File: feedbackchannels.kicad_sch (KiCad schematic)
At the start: 81 parts, among them J18 FB CH1, J19 FB CH2, J20 FB CH3, J21 FB CH4, J22 VDET CH1, J23 VDET CH2, U21 TLP2366, U22 TLP2366, U23 TLP2366, U24 TLP2366, U25 TLP2366, U26 TLP2366, U27 TLV7031, U28 TLV7031, U30 TLP2366, U31 TLP2366, U32 74LVC1G126, U34 PCA9534, U35 SN74LVC541A

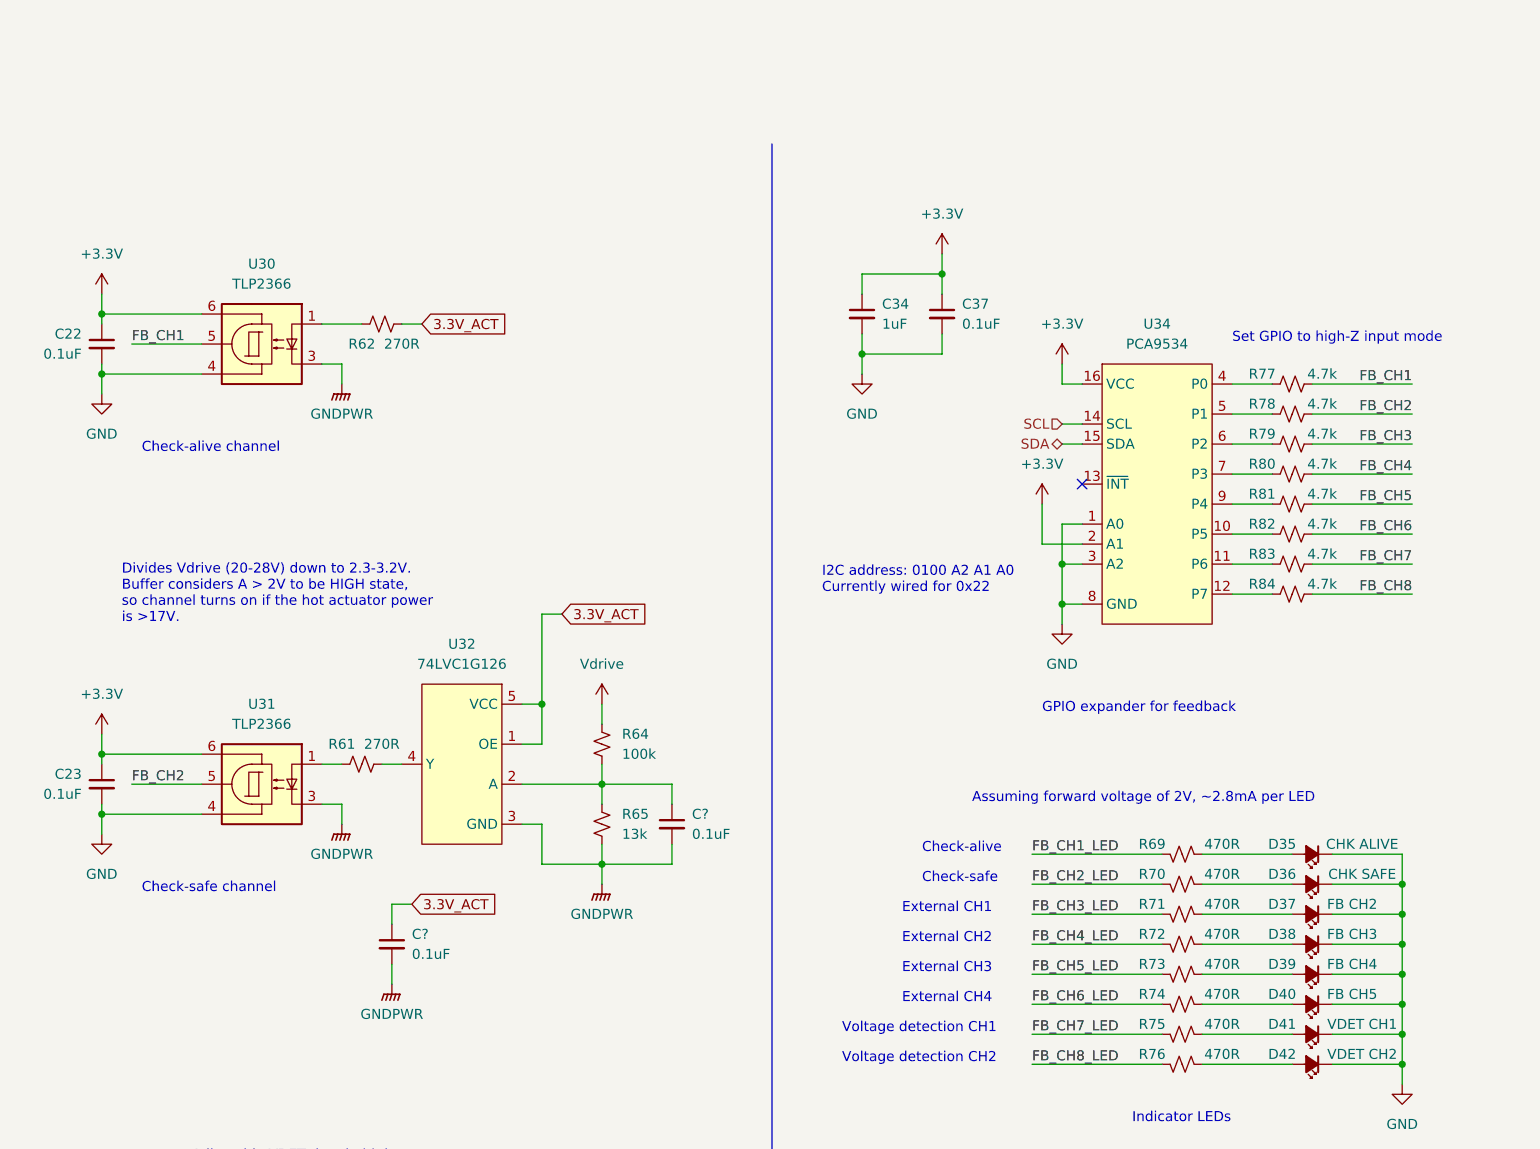
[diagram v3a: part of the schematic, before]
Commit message: LED MPNs and new status indicator
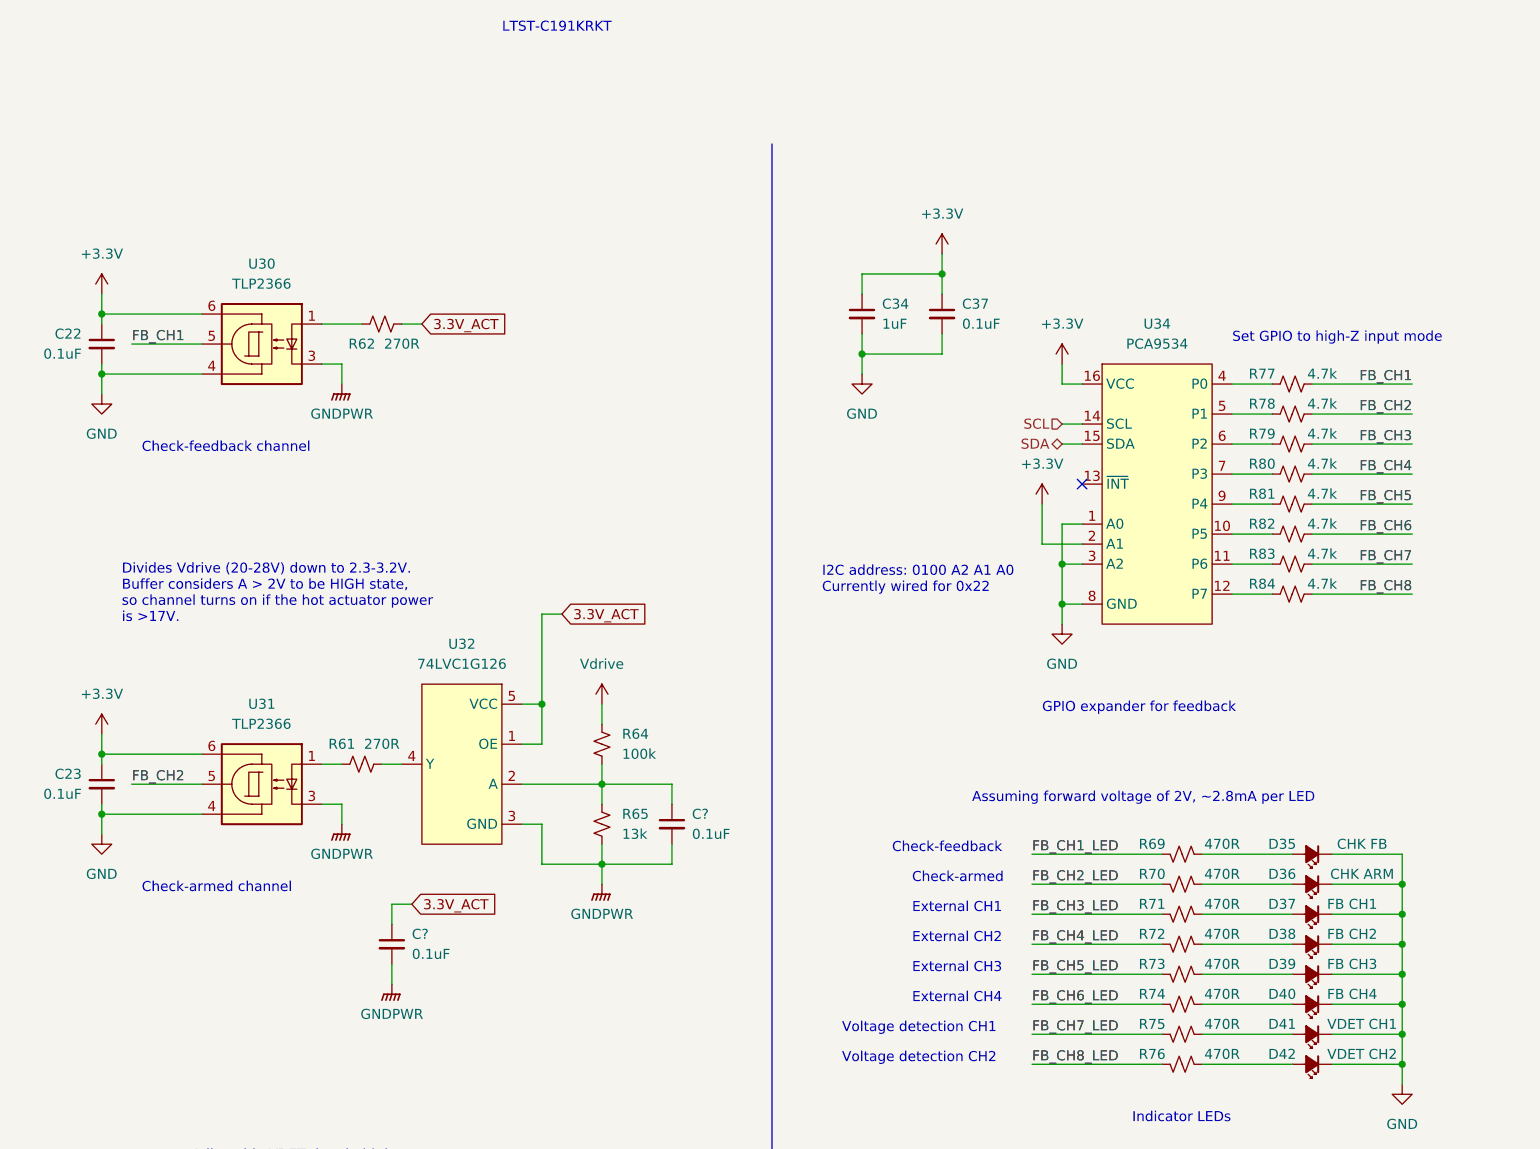
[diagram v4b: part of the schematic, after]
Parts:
- D35: value CHK ALIVE -> CHK FB; MPN (none) -> LTST-C191KGKT
- D36: value CHK SAFE -> CHK ARM; MPN (none) -> LTST-C191KFKT
- D37: value FB CH2 -> FB CH1; MPN (none) -> LTST-C191TBKT
- D38: value FB CH3 -> FB CH2; MPN (none) -> LTST-C191TBKT
- D39: value FB CH4 -> FB CH3; MPN (none) -> LTST-C191TBKT
- D40: value FB CH5 -> FB CH4; MPN (none) -> LTST-C191TBKT
- D41, D42: MPN (none) -> LTST-C191TBKT
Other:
- note added: "Check-armed"
- note added: "Check-armed channel"
- note added: "Check-feedback"
- note added: "Check-feedback channel"
- note added: "LTST-C191KRKT"
- note removed: "Check-alive"
- note removed: "Check-alive channel"
- note removed: "Check-safe"
- note removed: "Check-safe channel"

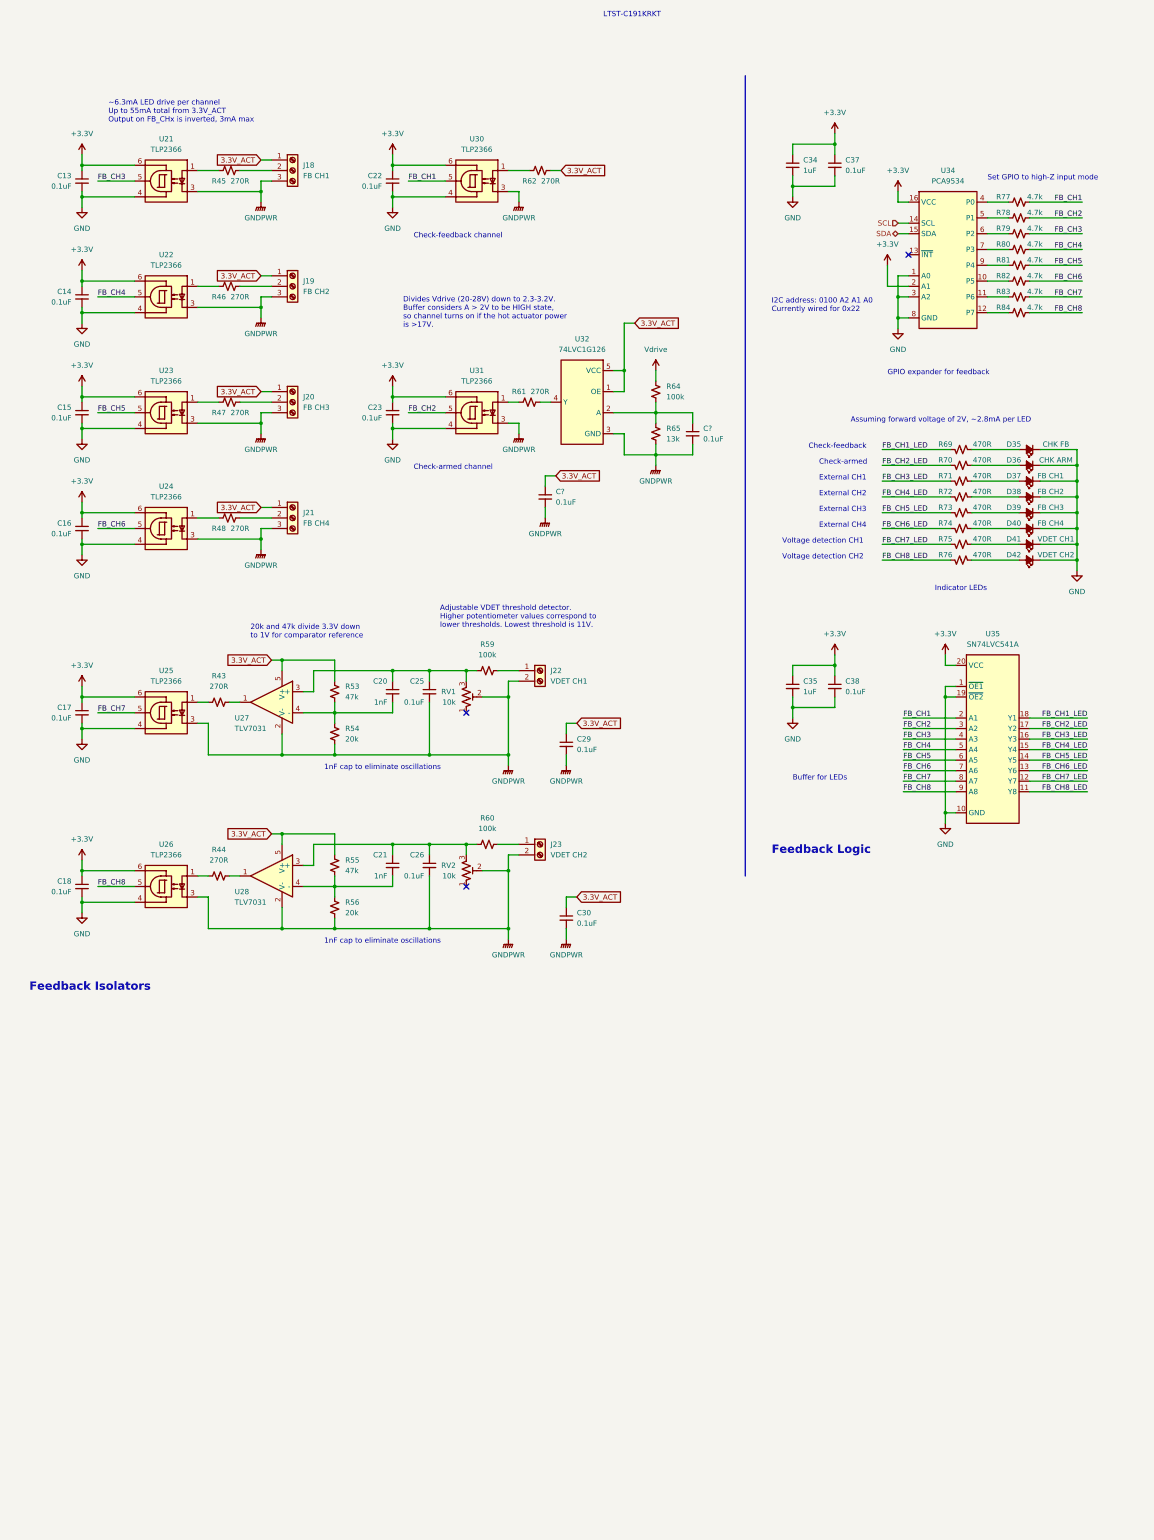
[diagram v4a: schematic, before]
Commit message: Safing jumper, status LEDs, better naming of power states
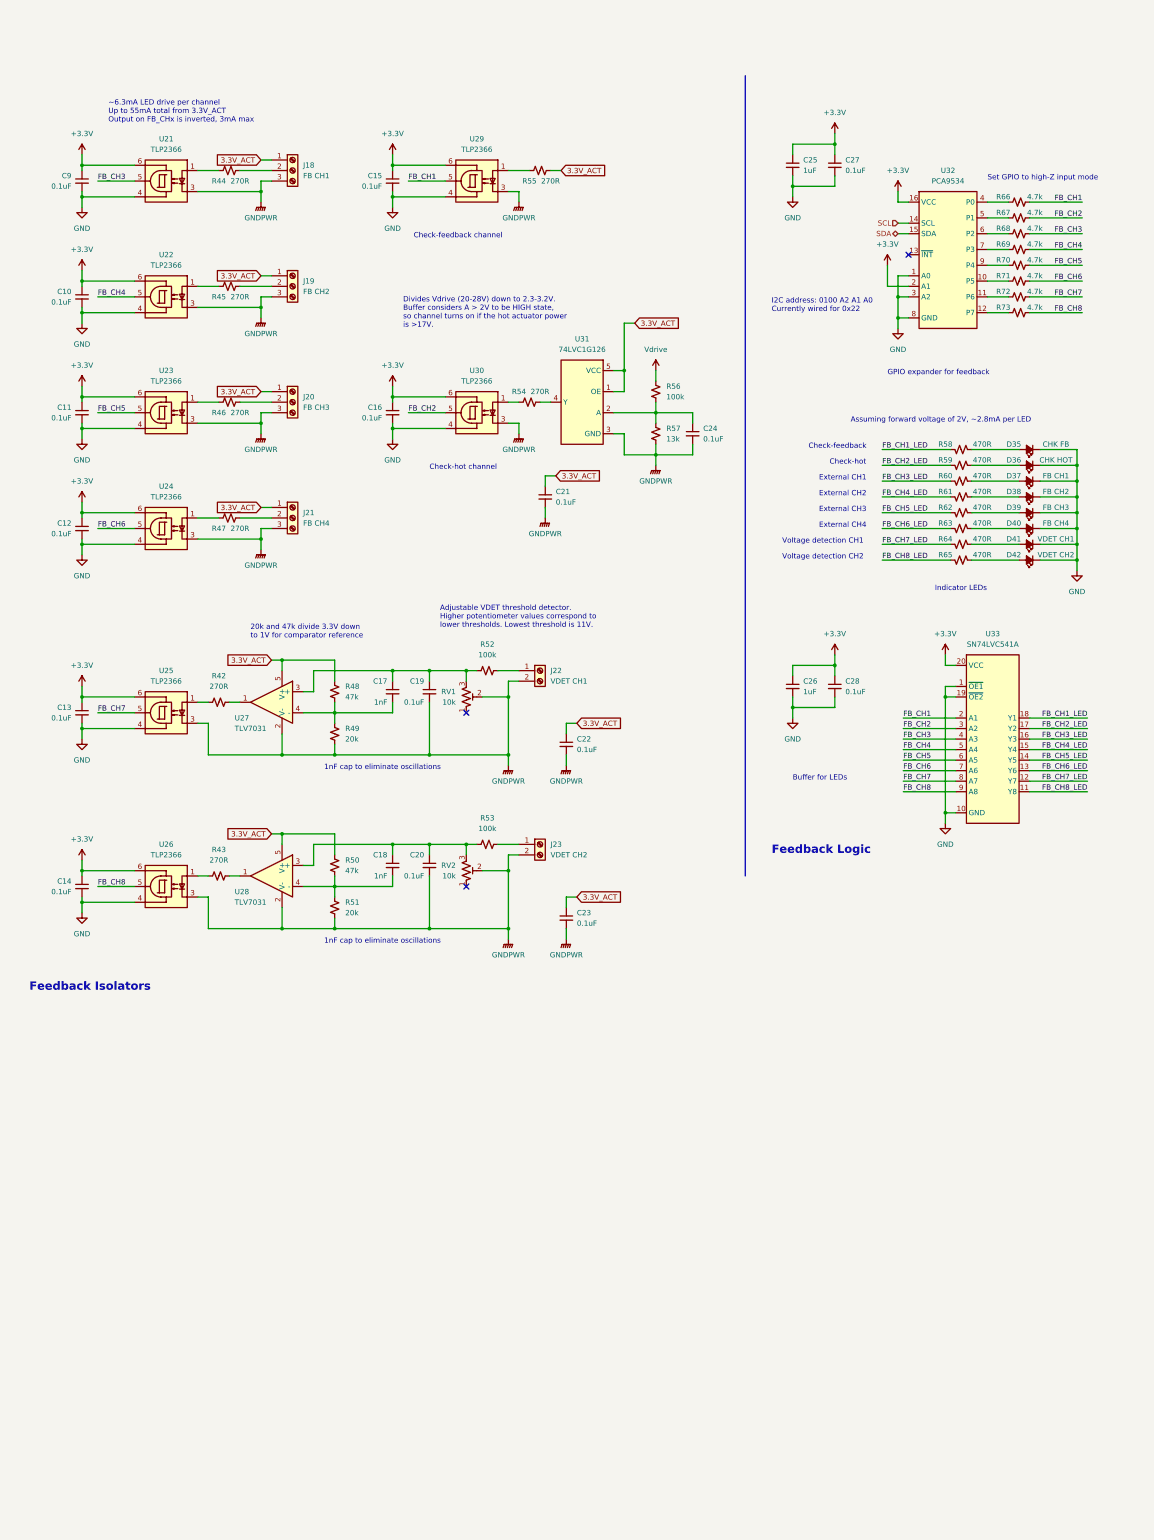
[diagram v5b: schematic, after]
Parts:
- D36: value CHK ARM -> CHK HOT; MPN LTST-C191KFKT -> LTST-C191KRKT
- gave numbers to parts that had none: 2
- renumbered C14 to C10, C15 to C11, C16 to C12, C17 to C13, C18 to C14, C22 to C15, C23 to C16, C20 to C17, C21 to C18, C25 to C19, C26 to C20, C29 to C22, C30 to C23, C34 to C25, C35 to C26, C37 to C27, C38 to C28, C13 to C9, R43 to R42, R44 to R43, R45 to R44, R46 to R45, R47 to R46, R48 to R47, R53 to R48, R54 to R49, R55 to R50, R56 to R51, R59 to R52, R60 to R53, R61 to R54, R62 to R55, R64 to R56, R65 to R57, R69 to R58, R70 to R59, R71 to R60, R72 to R61, R73 to R62, R74 to R63, R75 to R64, R76 to R65, R77 to R66, R78 to R67, R79 to R68, R80 to R69, R81 to R70, R82 to R71, R83 to R72, R84 to R73, U30 to U29, U31 to U30, U32 to U31, U34 to U32, U35 to U33
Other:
- note added: "Check-hot"
- note added: "Check-hot channel"
- note removed: "Check-armed"
- note removed: "Check-armed channel"
- note removed: "LTST-C191KRKT"

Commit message: Fixing up footprints
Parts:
- R42, R43, R44, R45, R46, R47, R54, R55: MPN (none) -> RC0603FR-07270RL

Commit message: MPN reassignment
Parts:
- RV1, RV2: footprint Resistor_SMD:R_0603_1608Metric -> Potentiometer_SMD:Potentiometer_Bourns_3224W_Vertical; MPN (none) -> 3224W-1-103E
